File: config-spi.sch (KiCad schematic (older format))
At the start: 38 parts, among them J1 0878311420, Q7 BSS138APW, Q8 BSS138APW, U1 XC7K70T-FBG484, U3 S25FL128SAGNFI000

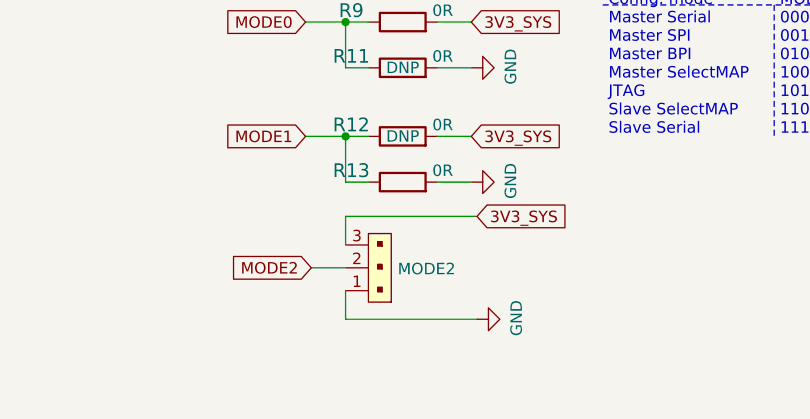
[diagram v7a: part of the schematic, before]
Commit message: Change mode jumper to 2.54 mm pitch
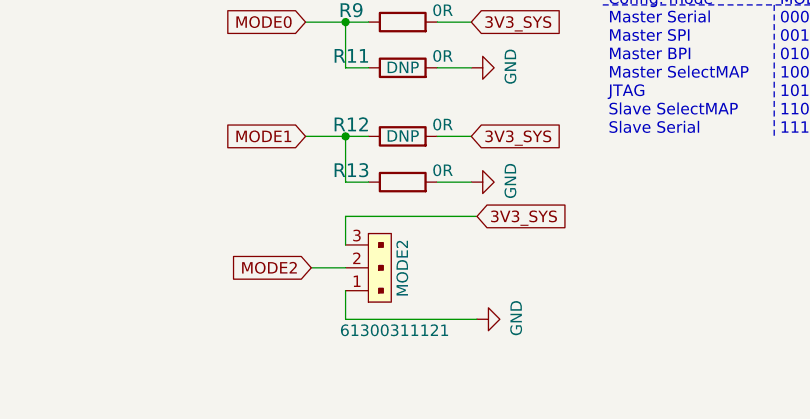
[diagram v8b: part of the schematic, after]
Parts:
- removed MODE2: 62000311121, lpddr4-test-board-footprints:62000311121, symbol lpddr4-test-board:62000311121
- added MODE2: 61300311121, lpddr4-test-board-footprints:PinHeader_1x3_P2.54_Drill1.1mm, symbol lpddr4-test-board:61300311121
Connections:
- net 3V3_SYS: now also MODE2.3
- net GND: now also MODE2.1
- net MODE2: now also MODE2.2
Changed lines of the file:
@@
 Title "LPDDR4 Test Board"
 Date ""
-Rev "1.0.1"
+Rev "1.0.2"
 Comp ""
 Comment1 ""
@@
 	0    -1   1    0
 $EndComp
-$Comp
-L lpddr4-test-board:62000311121 MODE2
-U 1 1 6148AC57
-P 8700 10050
-F 0 "MODE2" H 8622 10055 50  0000 R CNN
-F 1 "62000311121" H 8750 9850 50  0001 C CNN
-F 2 "lpddr4-test-board-footprints:62000311121" H 8800 10300 60  0001 L CNN
-F 3 "https://www.we-online.com/catalog/datasheet/62000311121.pdf" H 8900 10350 60  0001 L CNN
-F 4 "62000421121" H 8900 10550 60  0001 L CNN "MPN"
-F 5 "Wurth Elektronik" H 8900 11150 60  0001 L CNN "Manufacturer"
-	1    8700 10050
-	-1   0    0    1
-$EndComp
 Wire Wire Line
 	8550 8975 8650 8975
@@
 Text GLabel 5700 3150 1    50   Input ~ 0
 3V3_SYS
+$Comp
+L lpddr4-test-board:61300311121 J?
+U 1 1 6001B7F4
+P 8700 10150
+AR Path="/60225B0C/6001B7F4" Ref="J?"  Part="1"
+AR Path="/5FD53C7D/6001B7F4" Ref="MODE2"  Part="1"
+F 0 "MODE2" H 8925 10050 50  0000 R CNN
+F 1 "61300311121" V 8525 10325 50  0000 R CNN
+F 2 "lpddr4-test-board-footprints:PinHeader_1x3_P2.54_Drill1.1mm" H 8900 10350 60  0001 L CNN
+F 3 "https://katalog.we-online.de/em/datasheet/6130xx11121.pdf" H 8900 10450 60  0001 L CNN
+F 4 "61300311121" H 8900 10650 60  0001 L CNN "MPN"
+F 5 "Wurth Electronics Inc." H 8900 11250 60  0001 L CNN "Manufacturer"
+	1    8700 10150
+	0    -1   -1   0
+$EndComp
 $EndSCHEMATC
